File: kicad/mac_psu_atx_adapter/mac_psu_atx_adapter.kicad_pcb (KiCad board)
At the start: 2 copper layers, 6 parts, among them J1 Molex-15247100, J2 Molex-39299247, U1 74LVC1G04

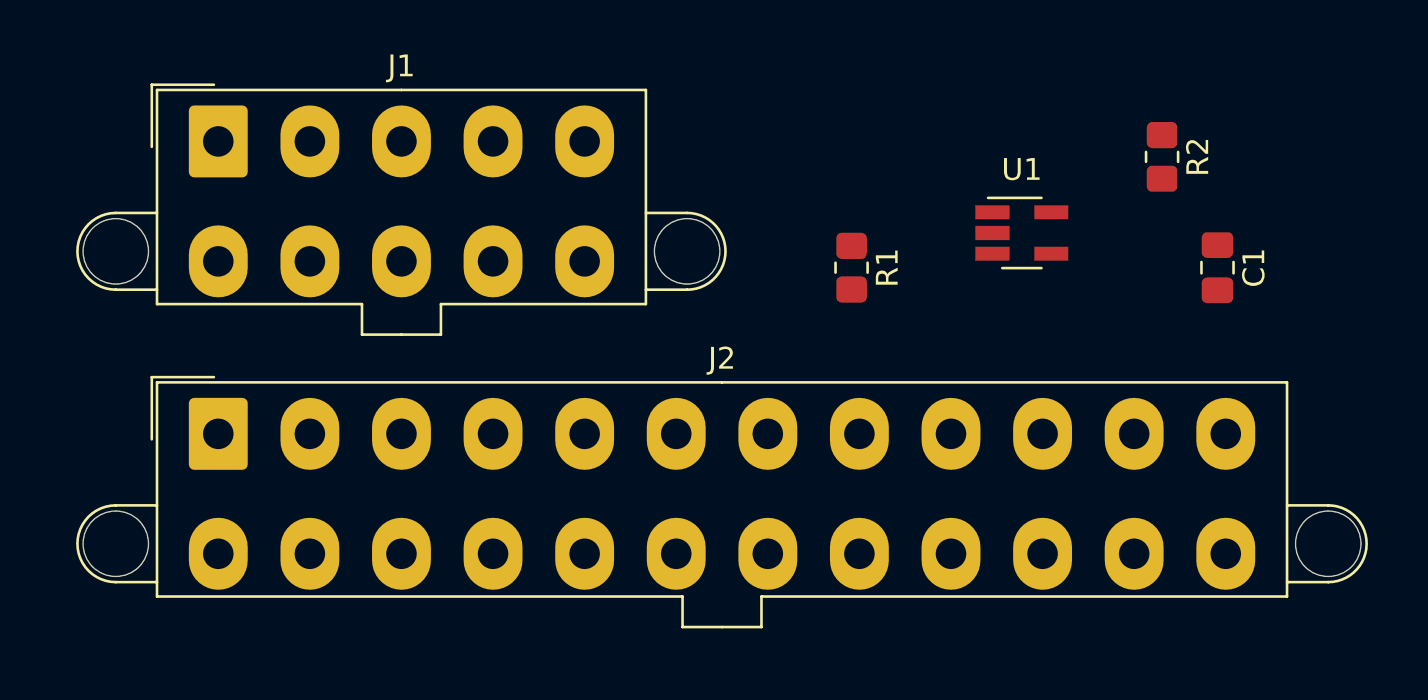
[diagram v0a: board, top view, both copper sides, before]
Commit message: Fix Molex-15247100 footprint
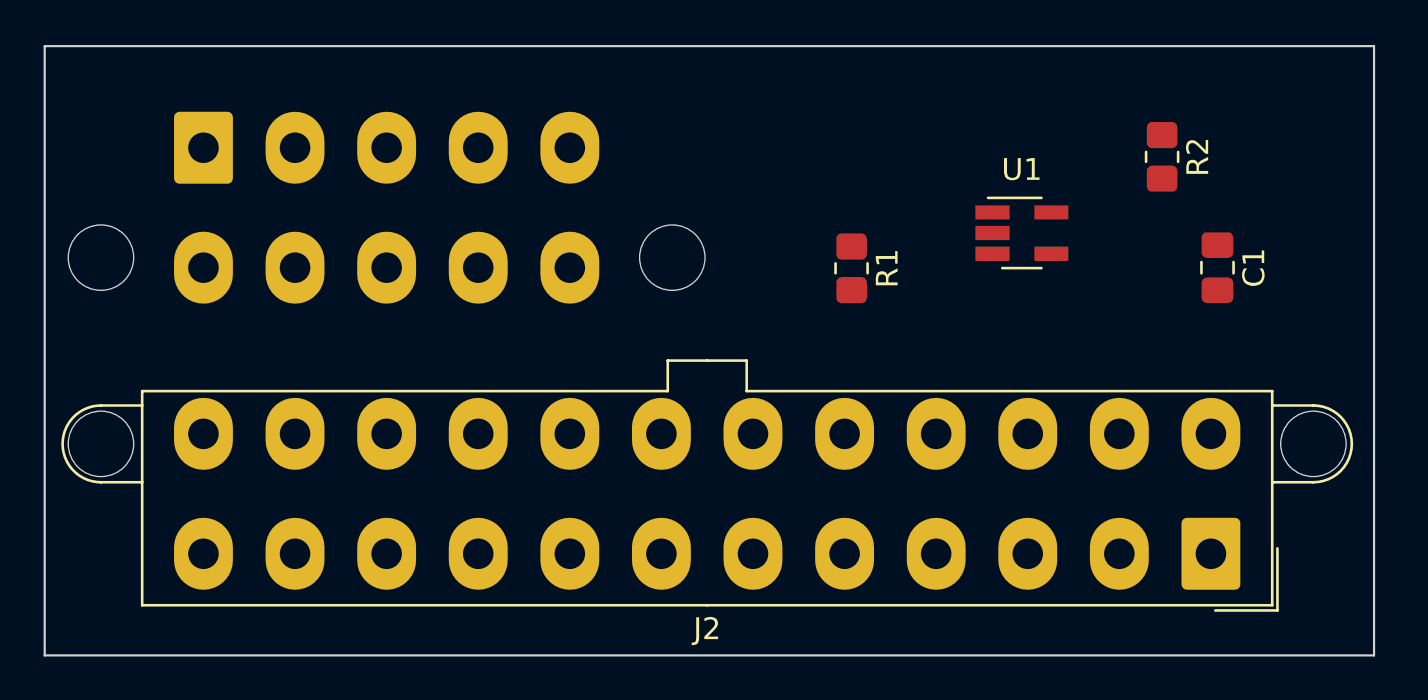
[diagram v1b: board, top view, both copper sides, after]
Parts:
- J1: footprint Connector_Molex:Molex_Mini-Fit_Jr_5566-10A2_2x05_P4.20mm_Vertical -> Local:Molex_Mini-Fit_Jr_15247100; moved to B.Cu
- moved J2 45.9 mm to (164.8, 107.1), turned to 180 degrees
- moved J1 16.1 mm to (135.4, 88.5), turned to 180 degrees
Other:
- board outline added: 61 x 27.9 mm

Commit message: Add route tracks
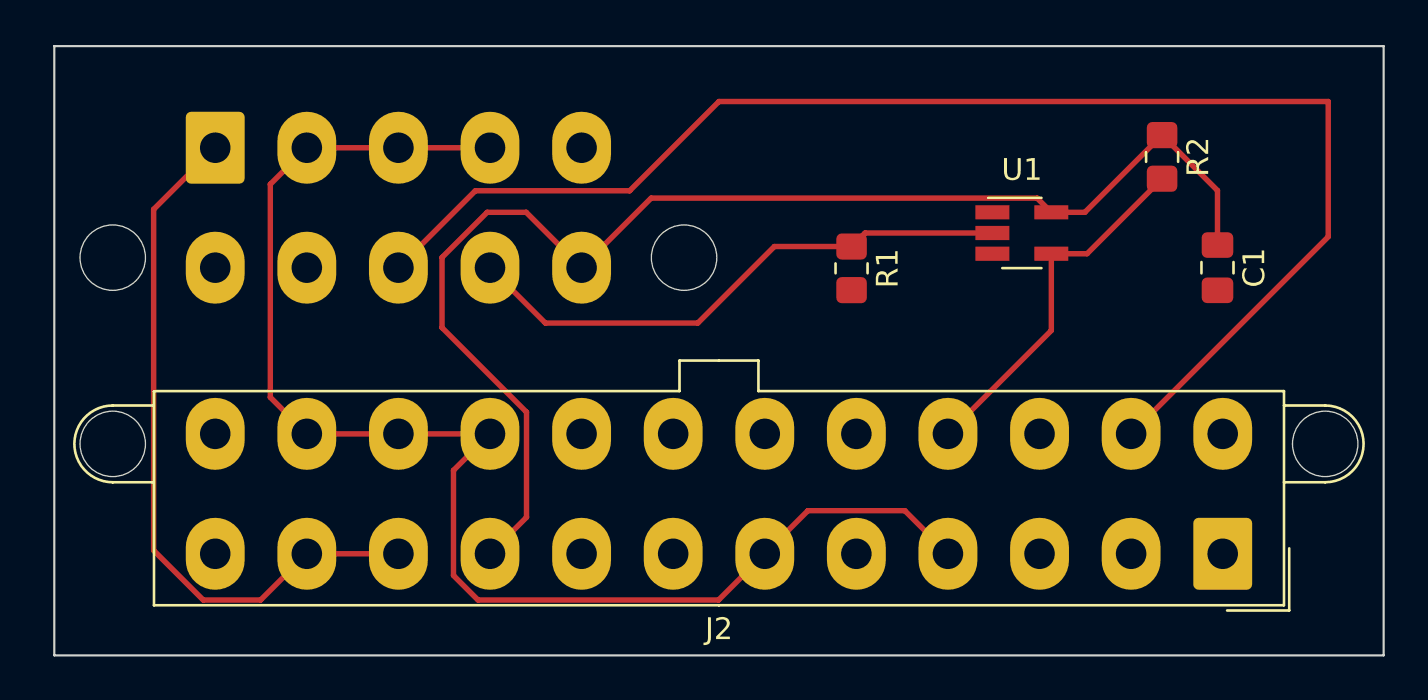
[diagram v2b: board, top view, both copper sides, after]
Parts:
- moved J1 0.54 mm to (135.9, 88.5)
- moved J2 0.54 mm to (165.3, 107.1)
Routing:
- net -12V: track 0.00 -> 64.8 mm
- net +5V: track 0.00 -> 64.2 mm
- net +5VSB: track 0.00 -> 60.0 mm
- net +12V: track 0.00 -> 32.7 mm
- net Net-(J1-Pin_9): track 0.00 -> 25.8 mm
- net PS_ON: track 0.00 -> 16.7 mm
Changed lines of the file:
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@@
   )
   (footprint "Connector_Molex:Molex_Mini-Fit_Jr_5566-24A2_2x12_P4.20mm_Vertical" (layer "F.Cu")
-    (at 164.8 107.1 180)
+    (at 165.34 107.1 180)
     (descr "Molex Mini-Fit Jr. Power Connectors, old mpn/engineering number: 5566-24A2, example for new mpn: 39-28-924x, 12 Pins per row, Mounting: Snap-in Plastic Peg PCB Lock (http://www.molex.com/pdm_docs/sd/039289068_sd.pdf), generated with kicad-footprint-generator")
     (tags "connector Molex Mini-Fit_Jr side entryplastic_peg")
@@
   )
   (footprint "Local:Molex_Mini-Fit_Jr_15247100" (layer "B.Cu")
-    (at 135.4 88.48 180)
+    (at 135.94 88.48 180)
     (descr "Molex Mini-Fit Jr. Power Connectors, old mpn/engineering number: 5566-10A2, example for new mpn: 39-28-910x, 5 Pins per row, Mounting: Snap-in Plastic Peg PCB Lock (http://www.molex.com/pdm_docs/sd/039289068_sd.pdf), generated with kicad-footprint-generator")
     (tags "connector Molex Mini-Fit_Jr side entryplastic_peg")
@@
     )
   )
-  (gr_rect (start 111.32 83.82) (end 172.28 111.76)
+  (gr_rect (start 111.76 83.82) (end 172.72 111.76)
     (stroke (width 0.1) (type default)) (fill none) (layer "Edge.Cuts"))
+  (segment (start 129.54 96.731192) (end 133.415 100.606192) (width 0.25) (layer "F.Cu") (net 1))
+  (segment (start 139.13 90.79) (end 156.83 90.79) (width 0.25) (layer "F.Cu") (net 1))
+  (segment (start 135.94 93.98) (end 139.13 90.79) (width 0.25) (layer "F.Cu") (net 1))
+  (segment (start 157.48 91.44) (end 159.02 91.44) (width 0.25) (layer "F.Cu") (net 1))
+  (segment (start 133.415 105.425) (end 131.74 107.1) (width 0.25) (layer "F.Cu") (net 1))
+  (segment (start 131.611192 91.44) (end 129.54 93.511192) (width 0.25) (layer "F.Cu") (net 1))
+  (segment (start 133.415 100.606192) (end 133.415 105.425) (width 0.25) (layer "F.Cu") (net 1))
+  (segment (start 159.02 91.44) (end 162.56 87.9) (width 0.25) (layer "F.Cu") (net 1))
+  (segment (start 129.54 93.511192) (end 129.54 96.731192) (width 0.25) (layer "F.Cu") (net 1))
+  (segment (start 133.4 91.44) (end 131.611192 91.44) (width 0.25) (layer "F.Cu") (net 1))
+  (segment (start 165.1 90.44) (end 165.1 92.9425) (width 0.25) (layer "F.Cu") (net 1))
+  (segment (start 156.83 90.79) (end 157.48 91.44) (width 0.25) (layer "F.Cu") (net 1))
+  (segment (start 135.94 93.98) (end 133.4 91.44) (width 0.25) (layer "F.Cu") (net 1))
+  (segment (start 162.56 87.9) (end 165.1 90.44) (width 0.25) (layer "F.Cu") (net 1))
+  (segment (start 121.22 109.22) (end 123.34 107.1) (width 0.25) (layer "F.Cu") (net 3))
+  (segment (start 119.14 88.48) (end 116.315 91.305) (width 0.25) (layer "F.Cu") (net 3))
+  (segment (start 118.591192 109.22) (end 121.22 109.22) (width 0.25) (layer "F.Cu") (net 3))
+  (segment (start 116.315 91.305) (end 116.315 106.943808) (width 0.25) (layer "F.Cu") (net 3))
+  (segment (start 116.315 106.943808) (end 118.591192 109.22) (width 0.25) (layer "F.Cu") (net 3))
+  (segment (start 123.34 107.1) (end 127.54 107.1) (width 0.25) (layer "F.Cu") (net 3))
+  (segment (start 121.665 99.925) (end 123.34 101.6) (width 0.25) (layer "F.Cu") (net 4))
+  (segment (start 130.065 108.093808) (end 131.191192 109.22) (width 0.25) (layer "F.Cu") (net 4))
+  (segment (start 131.74 101.6) (end 127.54 101.6) (width 0.25) (layer "F.Cu") (net 4))
+  (segment (start 121.665 90.155) (end 121.665 99.925) (width 0.25) (layer "F.Cu") (net 4))
+  (segment (start 150.765 105.125) (end 152.74 107.1) (width 0.25) (layer "F.Cu") (net 4))
+  (segment (start 142.22 109.22) (end 144.34 107.1) (width 0.25) (layer "F.Cu") (net 4))
+  (segment (start 123.34 88.48) (end 121.665 90.155) (width 0.25) (layer "F.Cu") (net 4))
+  (segment (start 131.74 101.6) (end 130.065 103.275) (width 0.25) (layer "F.Cu") (net 4))
+  (segment (start 123.34 88.48) (end 127.54 88.48) (width 0.25) (layer "F.Cu") (net 4))
+  (segment (start 131.74 88.48) (end 127.54 88.48) (width 0.25) (layer "F.Cu") (net 4))
+  (segment (start 144.34 107.1) (end 146.315 105.125) (width 0.25) (layer "F.Cu") (net 4))
+  (segment (start 130.065 103.275) (end 130.065 108.093808) (width 0.25) (layer "F.Cu") (net 4))
+  (segment (start 146.315 105.125) (end 150.765 105.125) (width 0.25) (layer "F.Cu") (net 4))
+  (segment (start 131.191192 109.22) (end 142.22 109.22) (width 0.25) (layer "F.Cu") (net 4))
+  (segment (start 123.34 101.6) (end 127.54 101.6) (width 0.25) (layer "F.Cu") (net 4))
+  (segment (start 142.24 86.36) (end 170.18 86.36) (width 0.25) (layer "F.Cu") (net 5))
+  (segment (start 127.54 93.98) (end 131.065 90.455) (width 0.25) (layer "F.Cu") (net 5))
+  (segment (start 131.065 90.455) (end 138.145 90.455) (width 0.25) (layer "F.Cu") (net 5))
+  (segment (start 170.18 92.56) (end 161.14 101.6) (width 0.25) (layer "F.Cu") (net 5))
+  (segment (start 138.145 90.455) (end 142.24 86.36) (width 0.25) (layer "F.Cu") (net 5))
+  (segment (start 170.18 86.36) (end 170.18 92.56) (width 0.25) (layer "F.Cu") (net 5))
+  (segment (start 141.27 96.52) (end 134.28 96.52) (width 0.25) (layer "F.Cu") (net 6))
+  (segment (start 148.32 93.01) (end 148.94 92.39) (width 0.25) (layer "F.Cu") (net 6))
+  (segment (start 148.94 92.39) (end 154.78 92.39) (width 0.25) (layer "F.Cu") (net 6))
+  (segment (start 134.28 96.52) (end 131.74 93.98) (width 0.25) (layer "F.Cu") (net 6))
+  (segment (start 144.78 93.01) (end 141.27 96.52) (width 0.25) (layer "F.Cu") (net 6))
+  (segment (start 148.32 93.01) (end 144.78 93.01) (width 0.25) (layer "F.Cu") (net 6))
+  (segment (start 157.48 96.86) (end 152.74 101.6) (width 0.25) (layer "F.Cu") (net 7))
+  (segment (start 159.12 93.34) (end 162.56 89.9) (width 0.25) (layer "F.Cu") (net 7))
+  (segment (start 157.48 93.34) (end 157.48 96.86) (width 0.25) (layer "F.Cu") (net 7))
+  (segment (start 157.48 93.34) (end 159.12 93.34) (width 0.25) (layer "F.Cu") (net 7))
 )

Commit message: Add GND zone
- Add 3D view PNG files
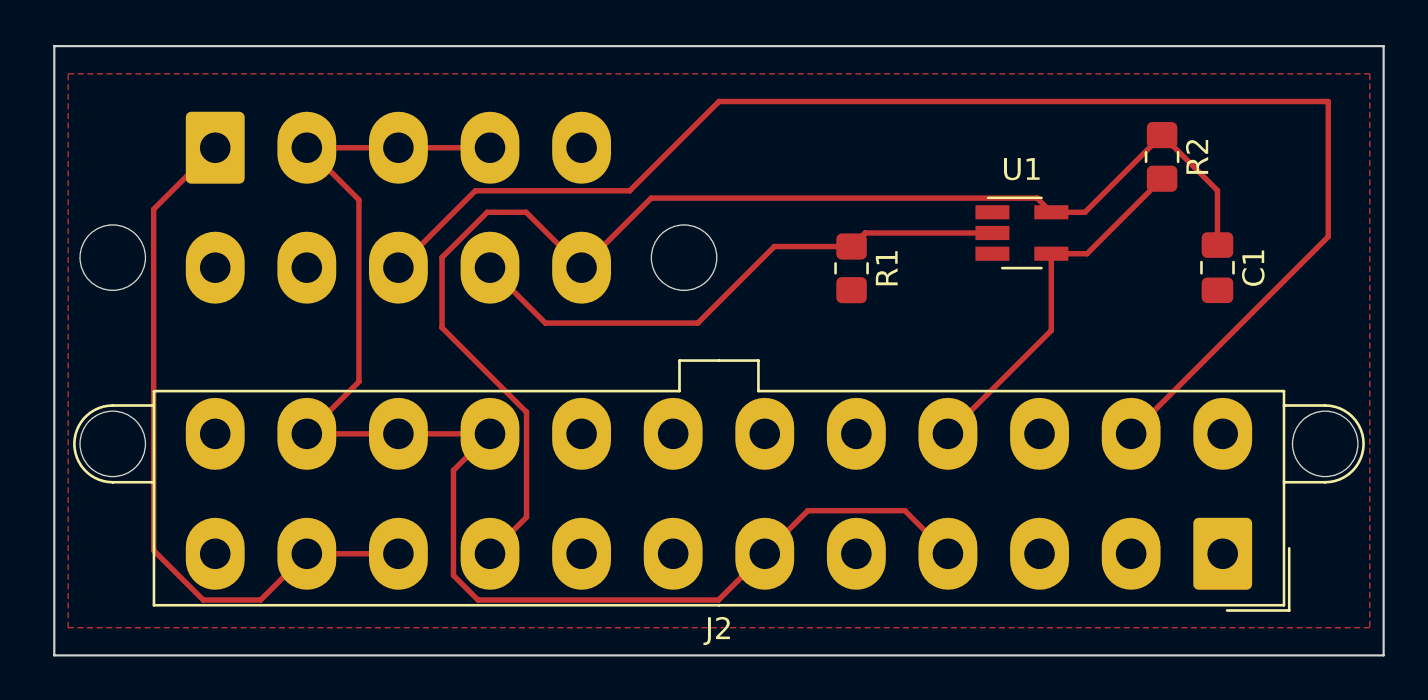
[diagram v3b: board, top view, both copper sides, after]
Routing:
- net +5V: track 64.2 -> 64.7 mm
- added copper zone on F.Cu, net GND
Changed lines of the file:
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@@
   (segment (start 116.315 106.943808) (end 118.591192 109.22) (width 0.25) (layer "F.Cu") (net 3))
   (segment (start 123.34 107.1) (end 127.54 107.1) (width 0.25) (layer "F.Cu") (net 3))
-  (segment (start 121.665 99.925) (end 123.34 101.6) (width 0.25) (layer "F.Cu") (net 4))
   (segment (start 130.065 108.093808) (end 131.191192 109.22) (width 0.25) (layer "F.Cu") (net 4))
   (segment (start 131.74 101.6) (end 127.54 101.6) (width 0.25) (layer "F.Cu") (net 4))
-  (segment (start 121.665 90.155) (end 121.665 99.925) (width 0.25) (layer "F.Cu") (net 4))
   (segment (start 150.765 105.125) (end 152.74 107.1) (width 0.25) (layer "F.Cu") (net 4))
+  (segment (start 125.73 99.21) (end 123.34 101.6) (width 0.25) (layer "F.Cu") (net 4))
   (segment (start 142.22 109.22) (end 144.34 107.1) (width 0.25) (layer "F.Cu") (net 4))
-  (segment (start 123.34 88.48) (end 121.665 90.155) (width 0.25) (layer "F.Cu") (net 4))
+  (segment (start 125.73 90.87) (end 125.73 99.21) (width 0.25) (layer "F.Cu") (net 4))
   (segment (start 131.74 101.6) (end 130.065 103.275) (width 0.25) (layer "F.Cu") (net 4))
   (segment (start 123.34 88.48) (end 127.54 88.48) (width 0.25) (layer "F.Cu") (net 4))
+  (segment (start 123.34 88.48) (end 125.73 90.87) (width 0.25) (layer "F.Cu") (net 4))
   (segment (start 131.74 88.48) (end 127.54 88.48) (width 0.25) (layer "F.Cu") (net 4))
   (segment (start 144.34 107.1) (end 146.315 105.125) (width 0.25) (layer "F.Cu") (net 4))
@@
   (segment (start 157.48 93.34) (end 157.48 96.86) (width 0.25) (layer "F.Cu") (net 7))
   (segment (start 157.48 93.34) (end 159.12 93.34) (width 0.25) (layer "F.Cu") (net 7))
+  (zone (net 2) (net_name "GND") (layer "F.Cu") (name "GND") (hatch edge 0.5)
+    (connect_pads (clearance 0.5))
+    (min_thickness 0.25) (filled_areas_thickness no)
+    (fill yes (thermal_gap 0.5) (thermal_bridge_width 0.5))
+    (polygon
+      (pts
+        (xy 112.395 85.09)
+        (xy 172.085 85.09)
+        (xy 172.085 110.49)
+        (xy 112.395 110.49)
+      )
+    )
+  )
 )
